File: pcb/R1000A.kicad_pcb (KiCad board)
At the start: 4 copper layers, 175 x 65.5 mm, 100 parts, among them J01 PCIESOCKET-X1, J02 PCIESOCKET-X1, J03 PCIESOCKET-X1, J04 PCIESOCKET-X1, J05 PCIESOCKET-X1, J06 PCIESOCKET-X1, J07 PCIESOCKET-X1, J08 PCIESOCKET-X1, J09 PCIESOCKET-X1, J1 CONN254P-01X06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

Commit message: updated layout and gerbers, moved C24 from under the bracket
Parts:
- moved C24 9.36 mm to (73.4, 134.1), turned to 0 degrees
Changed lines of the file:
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@@
   (general
     (links 680)
-    (no_connects 0)
+    (no_connects 1)
     (area 47.4 63.678571 233.500001 146.600001)
     (thickness 1.6)
     (drawings 65)
-    (tracks 2734)
+    (tracks 2728)
     (zones 0)
     (modules 100)
@@
     (visible_elements 7FFEFFFF)
     (pcbplotparams
-      (layerselection 0x010ff_80000007)
+      (layerselection 0x010fe_80000007)
       (usegerberextensions false)
       (excludeedgelayer true)
@@
   )
   (module Main:CAPC0603 (layer F.Cu)
-    (at 64.5 131.2 90)
+    (at 73.4 134.1)
     (descr "Resistor SMD 0603, reflow soldering, Vishay (see dcrcw.pdf)")
     (tags "resistor 0603")
     (attr smd)
-    (fp_text reference C24 (at 0 -1.27 90) (layer F.SilkS)
+    (fp_text reference C24 (at 0 -1.27) (layer F.SilkS) hide
       (effects (font (size 0.7 0.7) (thickness 0.15)))
     )
-    (fp_text value C0603 (at 0 0.508 90) (layer F.Fab)
+    (fp_text value C0603 (at 0 0.508) (layer F.Fab)
       (effects (font (size 0.127 0.127) (thickness 0.03)))
     )
@@
     (fp_line (start 0.5 0.675) (end -0.5 0.675) (layer F.SilkS) (width 0.15))
     (fp_line (start -0.5 -0.675) (end 0.5 -0.675) (layer F.SilkS) (width 0.15))
-    (pad 1 smd rect (at -0.7745 0 90) (size 0.787 0.864) (layers F.Cu F.Paste F.Mask)
+    (pad 1 smd rect (at -0.7745 0) (size 0.787 0.864) (layers F.Cu F.Paste F.Mask)
       (net 107 /PowerMonitor/LM5060_GATE))
-    (pad 2 smd rect (at 0.7745 0 90) (size 0.787 0.864) (layers F.Cu F.Paste F.Mask)
+    (pad 2 smd rect (at 0.7745 0) (size 0.787 0.864) (layers F.Cu F.Paste F.Mask)
       (net 2 GND))
     (model main.3dshapes/CAPC0603.wrl
@@
   (segment (start 135.9 87.775) (end 136.475 87.775) (width 0.15) (layer F.Cu) (net 106))
   (segment (start 135.6745 88.0005) (end 135.9 87.775) (width 0.15) (layer F.Cu) (net 106))
+  (segment (start 72.6255 134.1) (end 72.4205 133.895) (width 0.15) (layer F.Cu) (net 107) (status C00000))
+  (segment (start 72.4205 133.895) (end 66.725 133.895) (width 0.15) (layer F.Cu) (net 107) (status C00000))
   (segment (start 135.3 74.5) (end 135.175 74.5) (width 0.15) (layer In2.Cu) (net 107))
   (segment (start 51.7 75.475) (end 53.15 74.025) (width 0.15) (layer In2.Cu) (net 107))
   (segment (start 53.15 74.025) (end 134.7 74.025) (width 0.15) (layer In2.Cu) (net 107))
   (segment (start 63.4 133.1) (end 63.4 137.5) (width 0.15) (layer In2.Cu) (net 107))
-  (segment (start 64.5 132.7) (end 64.1 133.1) (width 0.15) (layer F.Cu) (net 107))
-  (segment (start 64.1 133.1) (end 63.4 133.1) (width 0.15) (layer F.Cu) (net 107))
   (via (at 63.4 133.1) (size 0.6) (drill 0.3) (layers F.Cu B.Cu) (net 107))
-  (segment (start 64.5 131.9745) (end 64.5 132.7) (width 0.15) (layer F.Cu) (net 107))
   (segment (start 51.7 137.2) (end 51.7 85.5) (width 0.15) (layer In2.Cu) (net 107))
   (segment (start 52.8 138.3) (end 51.7 137.2) (width 0.15) (layer In2.Cu) (net 107))
@@
   (segment (start 135.175 74.5) (end 134.7 74.025) (width 0.15) (layer In2.Cu) (net 107))
   (segment (start 135.4 85.1) (end 135.4 85) (width 0.15) (layer F.Cu) (net 107))
-  (segment (start 66.725 133.895) (end 66.725 133.425) (width 0.15) (layer F.Cu) (net 107))
-  (segment (start 64.5 132.8) (end 64.5 131.9745) (width 0.15) (layer F.Cu) (net 107))
-  (segment (start 64.8 133.1) (end 64.5 132.8) (width 0.15) (layer F.Cu) (net 107))
-  (segment (start 66.4 133.1) (end 64.8 133.1) (width 0.15) (layer F.Cu) (net 107))
-  (segment (start 66.725 133.425) (end 66.4 133.1) (width 0.15) (layer F.Cu) (net 107))
   (segment (start 131 86.6) (end 130.05 86.6) (width 0.15) (layer F.Cu) (net 108))
   (segment (start 129.7755 86.8745) (end 129.2 86.8745) (width 0.15) (layer F.Cu) (net 108))

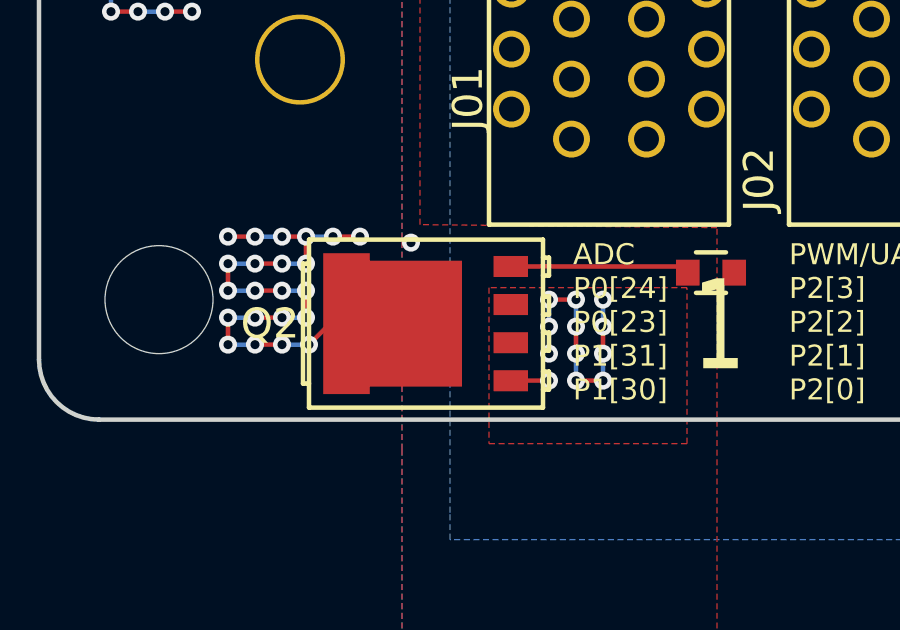
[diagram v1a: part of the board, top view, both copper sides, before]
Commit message: added mode thermal vias to FET source
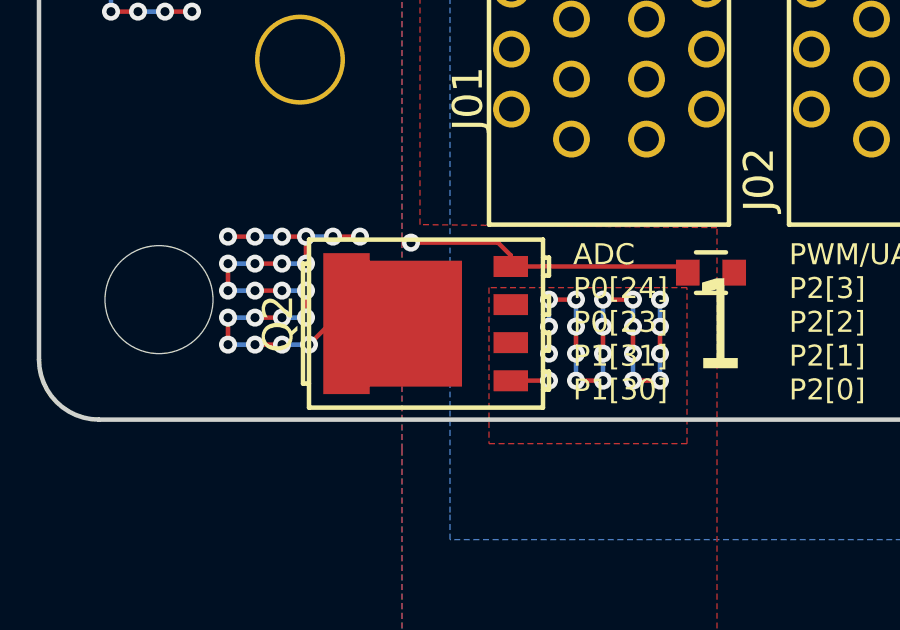
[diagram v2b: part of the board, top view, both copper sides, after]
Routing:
- net HT: track 285.2 -> 292.5 mm, vias 18 -> 26
- net /PowerMonitor/LM5060_GATE: track 180.5 -> 184.4 mm

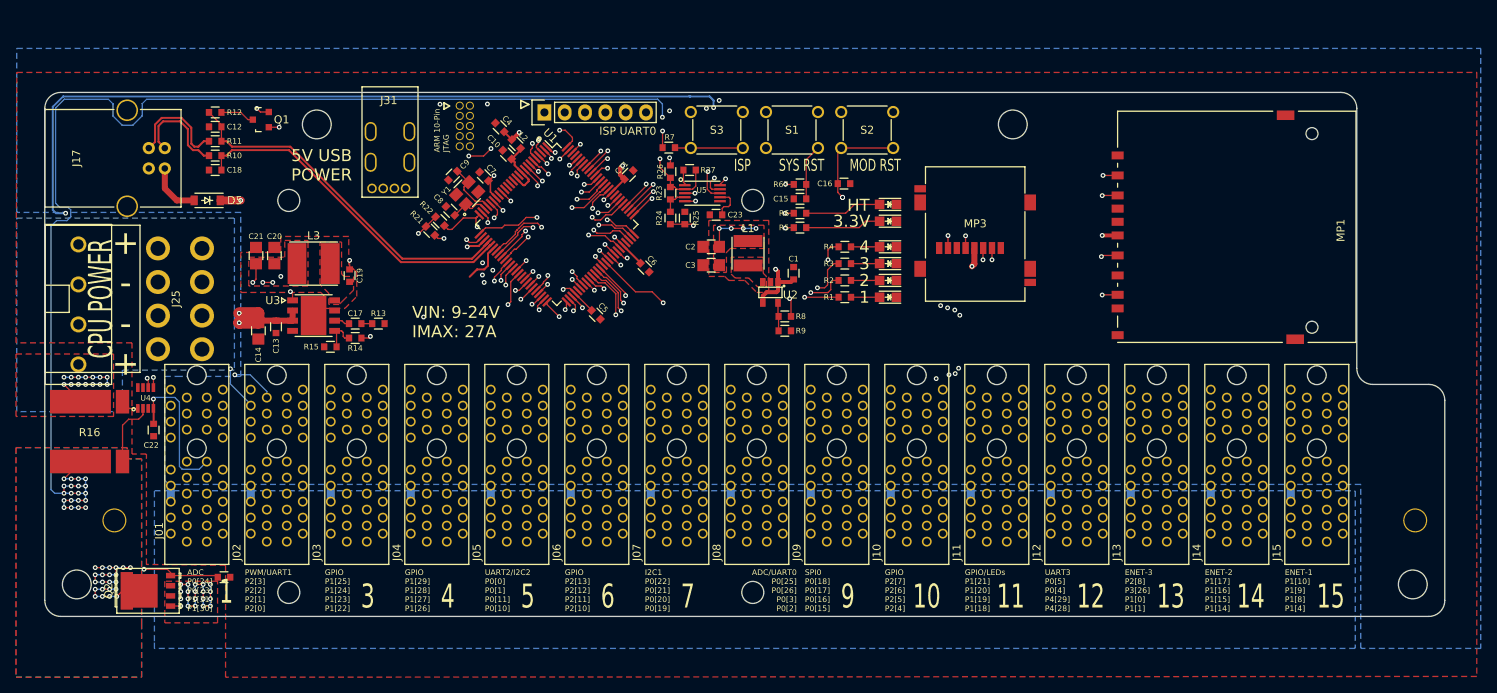
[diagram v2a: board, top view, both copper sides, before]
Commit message: removed UART header, moved LEDs to front, wip
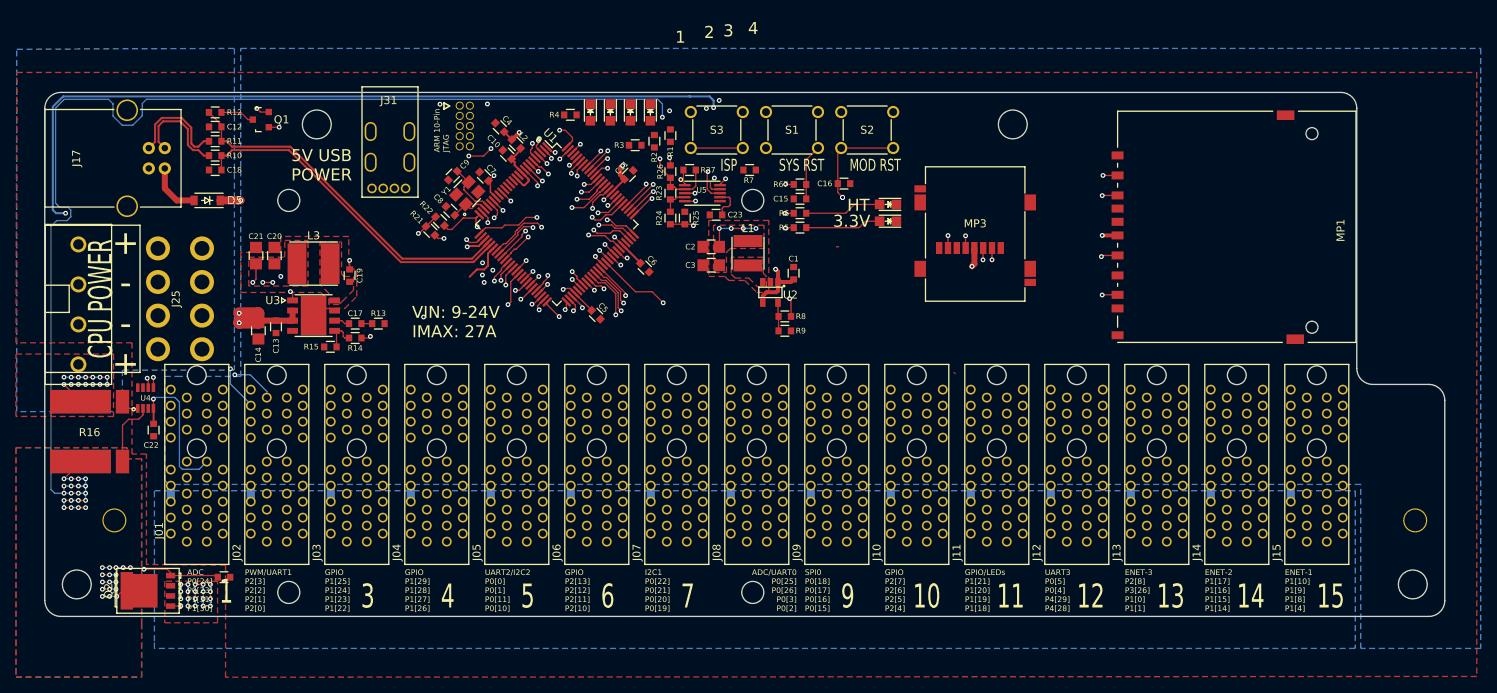
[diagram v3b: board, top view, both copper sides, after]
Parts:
- removed G***: LOGO, pluggee:pluggee-QRNEG-190X190
- removed G***: LOGO, pluggee:pluggee-LOGO-131X127
- removed J1: CONN254P-01X06, Main:SOCKET254P-01X06
- moved DLED4 40.8 mm to (119.2, 76.0), turned to 270 degrees
- moved DLED3 39.5 mm to (121.7, 76.0), turned to 270 degrees
- moved DLED2 38.4 mm to (124.2, 76.0), turned to 270 degrees
- moved R4 38.1 mm to (116.7, 76.3)
- moved DLED1 37.6 mm to (126.7, 76.0), turned to 270 degrees
- moved R3 30.1 mm to (124.8, 80.1), turned to 180 degrees
- moved R1 29.7 mm to (129.2, 78.9), turned to 90 degrees
- moved R2 29.5 mm to (127.2, 79.6), turned to 90 degrees
- moved R7 10.5 mm to (139.1, 83.2), turned to 0 degrees
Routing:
- net J11.PX3.A14.P1[19]: track 113.7 -> 81.2 mm, vias 4 -> 1
- net J11.PX1.A12.P1[21]: track 112.4 -> 80.8 mm, vias 4 -> 1
- net J11.PX4.A15.P1[18]: track 115.1 -> 83.7 mm, vias 4 -> 1
- net J11.PX2.A13.P1[20]: track 113.8 -> 82.8 mm, vias 4 -> 1
- net PFET_D: track 196.0 -> 179.3 mm, vias 44 -> 25
- net (no net): track 0.00 -> 11.0 mm, vias 0 -> 14
- net J08.PX3.A14.P0[3]: track 70.0 -> 60.7 mm
- net J08.PX4.A15.P0[2]: track 72.8 -> 65.1 mm
- net Net-(DLED4-Pad2): track 3.58 -> 0.00 mm
- net Net-(DLED3-Pad2): track 3.58 -> 0.00 mm
- net Net-(DLED2-Pad2): track 3.58 -> 0.00 mm
- net Net-(DLED1-Pad2): track 3.58 -> 0.00 mm
- net +3V3: track 67.9 -> 65.9 mm, vias 22 -> 21
- net J06.PX4.A15.P2[10]: track 53.2 -> 51.2 mm
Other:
- board text removed: "ISP UART0"

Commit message: wip, performing 1.1.1 fixes
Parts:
- moved R3 8.75 mm to (116.7, 76.8), turned to 0 degrees
- moved D5 3.47 mm to (70.8, 83.6)
- moved C18 2.49 mm to (74.7, 82.5), turned to 270 degrees
- moved R2 2.31 mm to (125.0, 80.3), turned to 180 degrees
- moved Q1 2.30 mm to (75.7, 76.9)
- moved R4 1.20 mm to (116.7, 75.1)
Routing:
- net J11.PX1.A12.P1[21]: track 80.8 -> 103.0 mm, vias 1 -> 2
- net J11.PX3.A14.P1[19]: track 81.2 -> 102.7 mm, vias 1 -> 2
- net J11.PX2.A13.P1[20]: track 82.8 -> 103.8 mm, vias 1 -> 2
- net J11.PX4.A15.P1[18]: track 83.7 -> 104.6 mm, vias 1 -> 2
- net /P2.9: track 59.2 -> 77.0 mm
- net +5V: track 18.0 -> 35.3 mm
- net Net-(DLED3-Pad2): track 0.00 -> 5.73 mm
- net Net-(DLED1-Pad2): track 0.00 -> 3.43 mm
- net /USB_5V+: track 6.79 -> 3.38 mm
- net Net-(DLED2-Pad2): track 0.00 -> 3.26 mm
- net Net-(DLED4-Pad2): track 0.00 -> 3.12 mm
- net J06.PX4.A15.P2[10]: track 51.2 -> 54.0 mm
- net Net-(Q1-Pad3): track 4.30 -> 2.35 mm
- net +3V3: track 65.9 -> 66.8 mm, vias 21 -> 22
- net /MCU_USB_D-: track 42.7 -> 42.1 mm

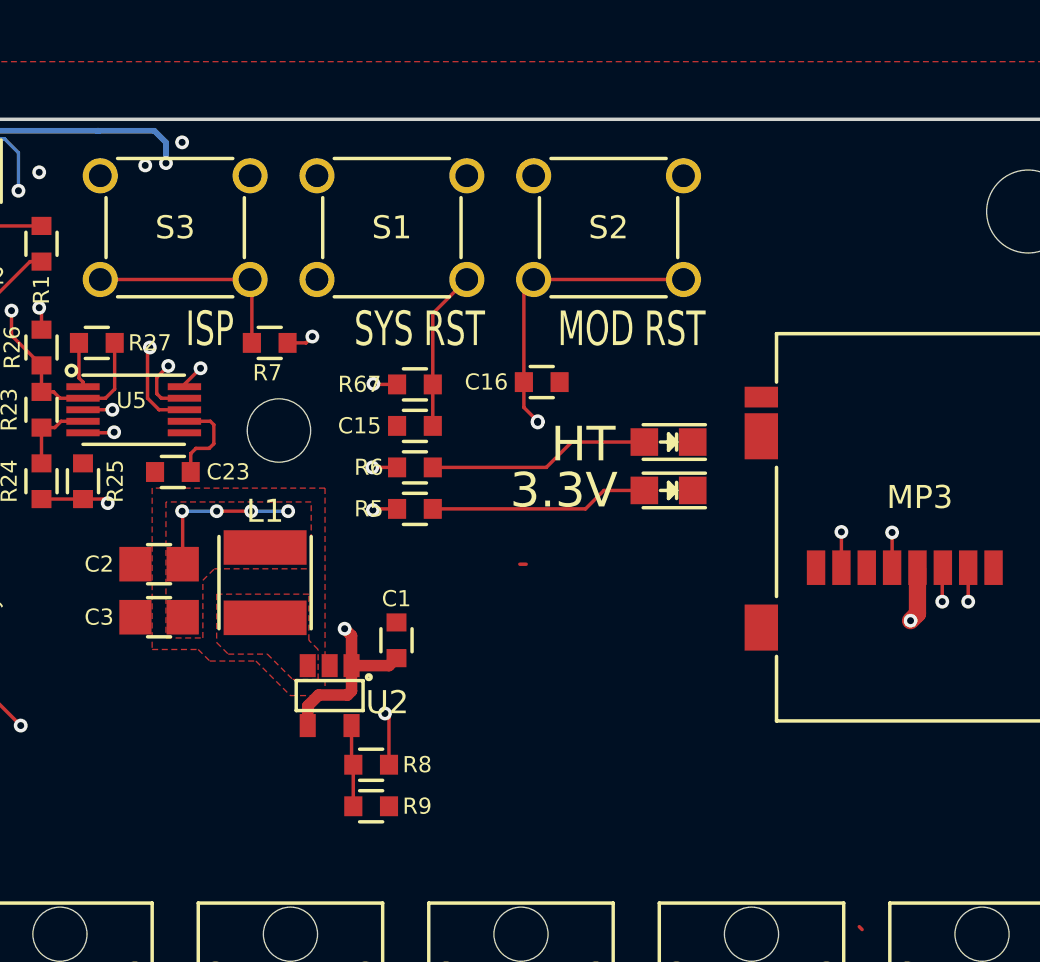
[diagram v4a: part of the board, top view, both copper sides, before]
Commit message: wip, need to add sense resistors for supplies
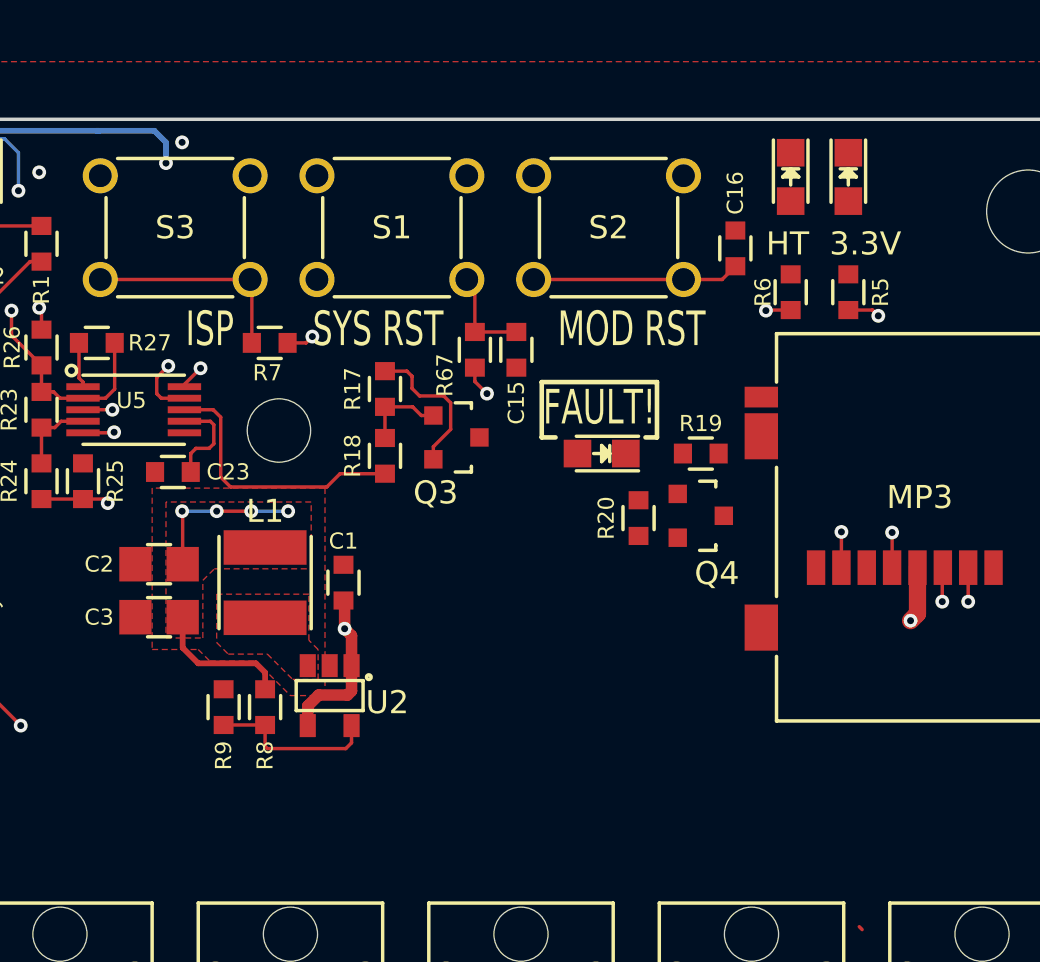
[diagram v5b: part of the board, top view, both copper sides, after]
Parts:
- added DLED5: Led_Small, Main:LED-0805, F.Cu at (153.5, 88.0)
- added Q3: Q_PNP_BEC, Main:SOT190P290X130X100-3, F.Cu at (147.2, 87.3)
- added Q4: Q_NPN_BEC, Main:SOT190P290X130X100-3, F.Cu at (157.8, 90.7)
- added R17: R0603, Main:RESC0603, F.Cu at (144.1, 85.2)
- added R18: R0603, Main:RESC0603, F.Cu at (144.1, 88.1)
- added R19: R0603, Main:RESC0603, F.Cu at (157.8, 88.0)
- added R20: R0603, Main:RESC0603, F.Cu at (155.1, 90.8)
- moved R5 21.0 mm to (164.2, 81.0), turned to 90 degrees
- moved R6 18.0 mm to (161.7, 81.0), turned to 90 degrees
- moved D1 15.7 mm to (164.2, 76.0), turned to 270 degrees
- moved D2 12.7 mm to (161.7, 76.0), turned to 270 degrees
- moved C16 10.2 mm to (159.3, 79.1), turned to 90 degrees
- moved R9 7.71 mm to (137.1, 99.0), turned to 90 degrees
- moved C15 5.50 mm to (149.8, 83.5), turned to 270 degrees
- moved R8 5.24 mm to (138.9, 99.0), turned to 270 degrees
- moved C1 3.40 mm to (142.3, 93.6)
- moved R67 3.00 mm to (148.0, 83.5), turned to 270 degrees
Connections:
- U5 pad 8: HV_~PGD -> CHIP_~PGD
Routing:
- net HV_~PGD: track 127.0 -> 0.23 mm, vias 2 -> 0
- net HT: track 292.5 -> 307.6 mm
- net CHIP_~PGD: track 0.00 -> 11.8 mm
- net Net-(D2-Pad2): track 9.63 -> 0.00 mm
- net Net-(D1-Pad2): track 9.51 -> 0.00 mm
- net PFET_D: track 179.3 -> 185.8 mm
- net +3V3: track 66.8 -> 71.2 mm, vias 22 -> 21
- net /Power/FB3V3: track 3.53 -> 7.37 mm
- net Net-(Q3-Pad1): track 0.00 -> 3.61 mm
- net /~RESET: track 52.1 -> 49.4 mm
- net ~MRESET: track 298.9 -> 301.6 mm, vias 3 -> 1
- net +5V: track 35.3 -> 34.5 mm
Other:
- board text added: "FAULT!"

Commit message: wip, adding to git
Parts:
- added C25: C0603, Main:CAPC0603, F.Cu at (152.4, 100.0)
- added C26: C0603, Main:CAPC0603, F.Cu at (155.3, 103.6)
- added C27: C0603, Main:CAPC0603, F.Cu at (147.9, 102.2)
- added R28: R1206, Main:RESC1206, F.Cu at (132.5, 97.7)
- added R29: R0603, Main:RESC0603, F.Cu at (130.2, 97.7)
- added R30: R1206, Main:RESC1206, F.Cu at (78.3, 96.5)
- added R31: R0603, Main:RESC0603, F.Cu at (76.4, 99.0)
- added R32: R0603, Main:RESC0603, F.Cu at (154.6, 99.5)
- added R33: R0603, Main:RESC0603, F.Cu at (152.4, 98.3)
- added R34: R0603, Main:RESC0603, F.Cu at (157.5, 104.1)
- added R35: R0603, Main:RESC0603, F.Cu at (145.7, 101.4)
- added R36: R0603, Main:RESC0603, F.Cu at (157.5, 102.4)
- added R37: R0603, Main:RESC0603, F.Cu at (145.7, 103.1)
- U4: value INA219AIDCNR -> INA3221AIRGVR; footprint Main:SOT065P195X120-8 -> Main:QFN65P400X400X90-16NT210X210
- moved U4 88.4 mm to (151.6, 103.6)
- moved C22 83.5 mm to (147.4, 105.2), turned to 180 degrees
- moved C1 13.1 mm to (135.3, 104.7), turned to 180 degrees
- moved R8 9.95 mm to (129.7, 102.8), turned to 0 degrees
- moved R9 9.28 mm to (129.7, 104.6), turned to 180 degrees
- moved C2 9.23 mm to (127.2, 98.7)
- moved C3 9.10 mm to (127.2, 100.8)
- moved U2 7.74 mm to (134.8, 102.0), turned to 180 degrees
- moved L1 4.85 mm to (136.3, 97.7)
- moved C20 2.51 mm to (78.7, 91.6)
- moved C21 2.47 mm to (76.5, 91.6)
- moved R16 1.00 mm to (57.6, 115.9), turned to 180 degrees
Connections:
- L1 pad 2: +3V3 -> 3V3+
- L3 pad 2: +5V -> 5V0+
- R16 pad 1: PFET_D -> HT_IN
- R16 pad 2: HT_IN -> PFET_D
- R16 pad 3: /PowerMonitor/IIN- -> /PowerMonitor/IIN+
- R16 pad 4: /PowerMonitor/IIN+ -> /PowerMonitor/IIN-
- U4 pad 1: /PowerMonitor/IIN+ -> /PowerMonitor/IN-3
- U4 pad 2: /PowerMonitor/IIN- -> /PowerMonitor/IN+3
- U4 pad 5: SCL0 -> GND
- U4 pad 6: SDA0 -> SCL0
- U4 pad 7: GND -> SDA0
- U4 pad 8: GND -> (no net)
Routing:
- net +3V3: track 71.2 -> 45.2 mm
- net +5V: track 34.5 -> 14.0 mm, vias 7 -> 5
- net HT_IN: track 16.7 -> 1.63 mm, vias 14 -> 0
- net (no net): track 10.7 -> 22.4 mm, vias 14 -> 28
- net SDA0: track 218.9 -> 210.2 mm, vias 3 -> 2
- net /PowerMonitor/IIN-: track 8.43 -> 0.00 mm
- net J13.PX1.A12.P2[8]: track 79.8 -> 87.9 mm, vias 1 -> 2
- net SCL0: track 232.9 -> 226.8 mm, vias 4 -> 3
- net PFET_D: track 185.8 -> 182.1 mm
- net /PowerMonitor/IIN+: track 2.60 -> 0.00 mm
- net /Power/FB3V3: track 7.37 -> 4.89 mm
- net J13.PX2.A13.P3[26]: track 104.2 -> 102.0 mm
- net J15.PX1.A12.P1[10]: track 108.3 -> 106.2 mm
- net J15.PX4.A15.P1[4]: track 111.7 -> 109.6 mm
- net J15.PX2.A13.P1[9]: track 110.9 -> 108.9 mm
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- added copper zone on F.Cu, net 3V3+
- added copper zone on F.Cu, net 5V0+

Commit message: layout wip
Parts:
- moved C24 76.1 mm to (136.0, 90.8)
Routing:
- net HT: track 307.6 -> 207.1 mm
- net (no net): track 22.4 -> 11.9 mm, vias 28 -> 14
- net /PowerMonitor/LM5060_GATE: track 184.4 -> 187.6 mm, vias 3 -> 4
- net PFET_D: track 182.1 -> 179.3 mm, vias 25 -> 22
- added copper zone on In1.Cu, net HT
- added copper zone on In1.Cu, net PFET_D
